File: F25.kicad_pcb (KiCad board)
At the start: 2 copper layers, 45 x 30 mm, 44 parts, among them J3 B2B-PH-K-S, J4 USB_C_Receptacle_USB2.0_16P, Q1 IRLML6244, SW1 RESET, SW2 BOOT, U1 MS5611-01BA, U2 MPU-6050, U4 ESP32-S3-WROOM-1-N8, U5 AP2112K-3.3

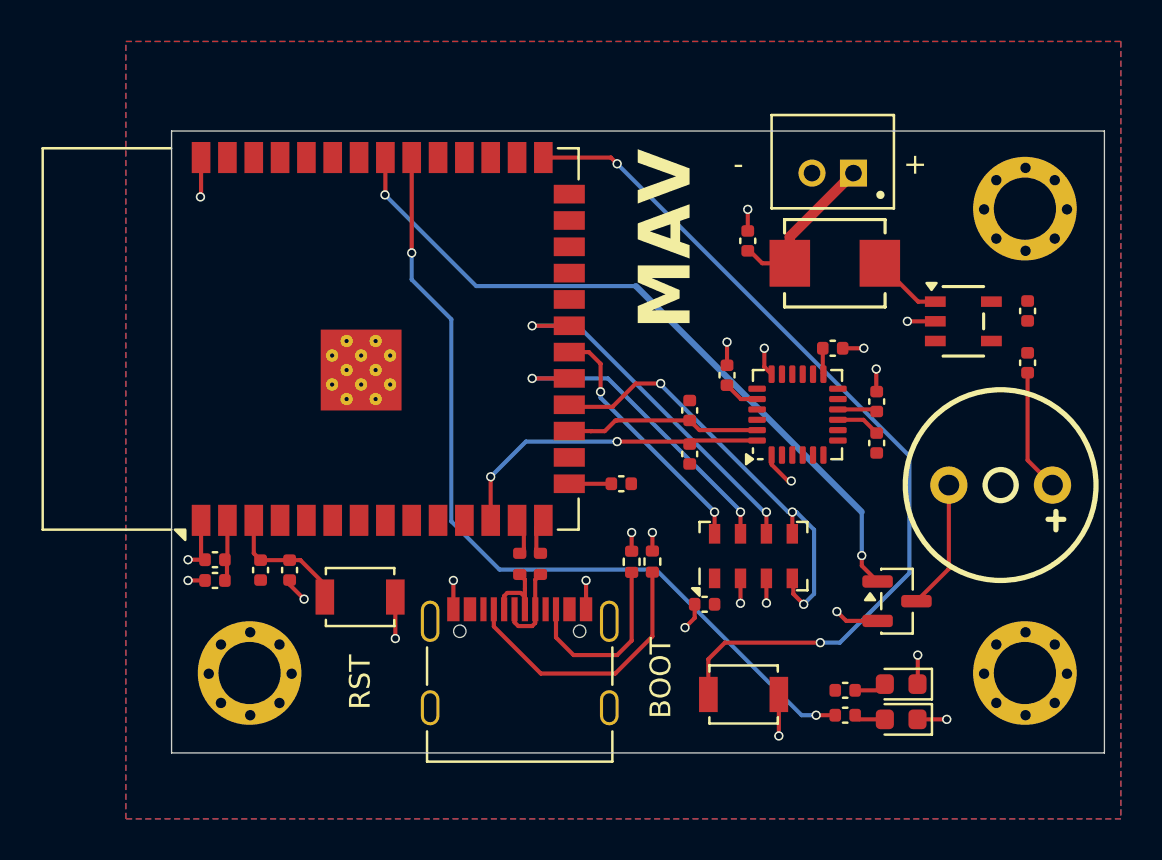
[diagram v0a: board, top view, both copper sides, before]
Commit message: Update LED Resistors
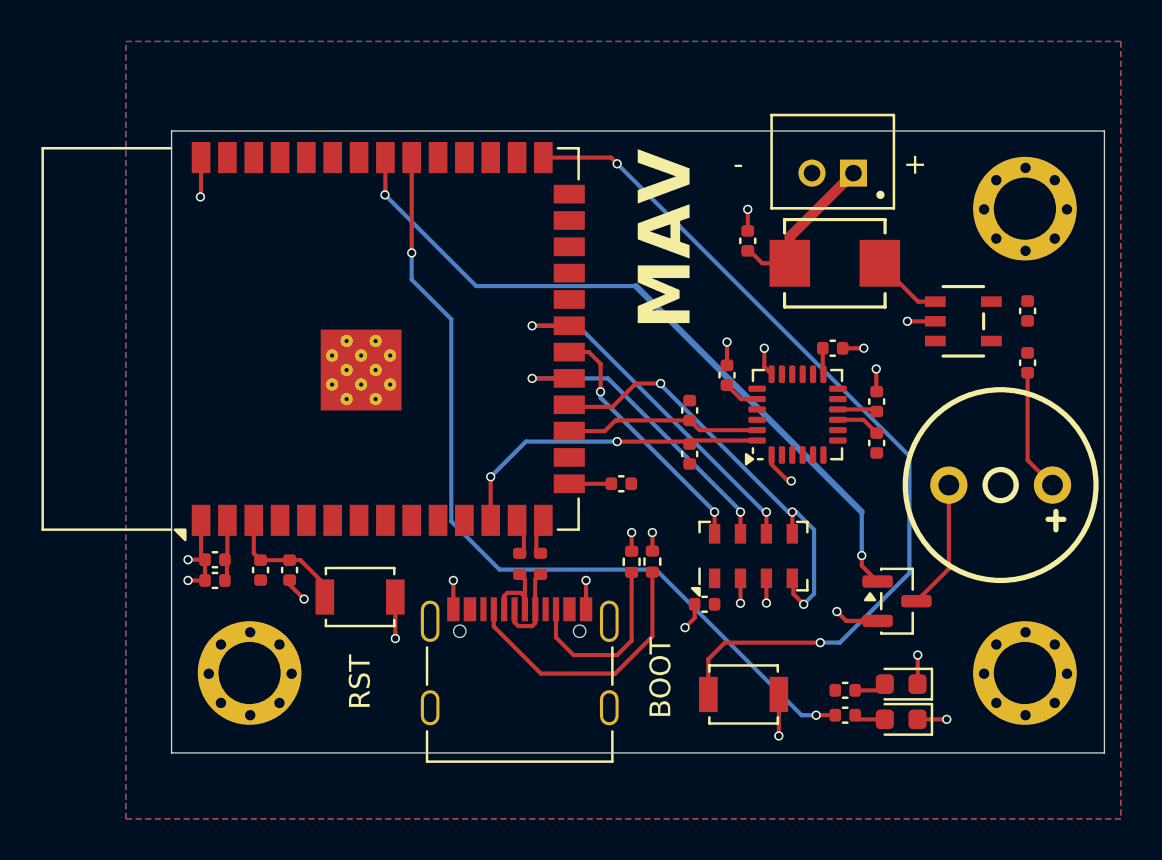
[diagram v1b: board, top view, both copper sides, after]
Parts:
- removed ?: , clipboard:8a0a766a-bff8-4b8c-9015-f6a2d7131c27
- R1: value 2k -> 270R
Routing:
- net BAT-: track 34.9 -> 35.9 mm

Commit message: LED Updates
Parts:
- R1: value 270R -> 120R
- R7: value 1.5k -> 820R
- moved G*** 0.44 mm to (154.6, 96.0)
- moved G*** 0.33 mm to (154.5, 93.0)
- moved G*** 0.32 mm to (153.0, 89.0)
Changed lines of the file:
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@@
 			)
 		)
-		(fp_text user "${REFERENCE}"
-			(at 0 -0.6 90)
-			(unlocked yes)
-			(layer "F.Fab")
-			(effects
-				(font
-					(size 1 1)
-					(thickness 0.15)
-				)
-			)
-		)
 		(pad "" smd rect
 			(at -2.9 1.06 90)
@@
 			)
 		)
-		(property "Value" "1.5k"
+		(property "Value" "820R"
 			(at 0 1.16 0)
 			(layer "F.Fab")
@@
 			)
 		)
-		(property "LCSC" "C25867"
+		(property "LCSC" "C25135"
 			(at 0 0 0)
 			(unlocked yes)
@@
 			)
 		)
-		(property "Value" "270R"
+		(property "Value" "120R"
 			(at 0 1.16 0)
 			(layer "F.Fab")
@@
 			)
 		)
-		(property "LCSC" "C25099"
+		(property "LCSC" "C25079"
 			(at 0 0 0)
 			(unlocked yes)
@@
 	(footprint "LOGO"
 		(layer "B.Cu")
-		(at 154.824101 93.082125)
+		(at 154.5 93)
 		(property "Reference" "G***"
 			(at 0 0 0)
@@
 	(footprint "LOGO"
 		(layer "B.Cu")
-		(at 155.024101 95.882125)
+		(at 154.6 96)
 		(property "Reference" "G***"
 			(at 0 0 0)
@@
 	(footprint "LOGO"
 		(layer "B.Cu")
-		(at 142.519024 94.578305)
+		(at 142.5 94.6)
 		(property "Reference" "G***"
 			(at 0 0 0)
@@
 	(footprint "LOGO"
 		(layer "B.Cu")
-		(at 153.1 89.3)
+		(at 153 89)
 		(property "Reference" "G***"
 			(at 0 0 0)

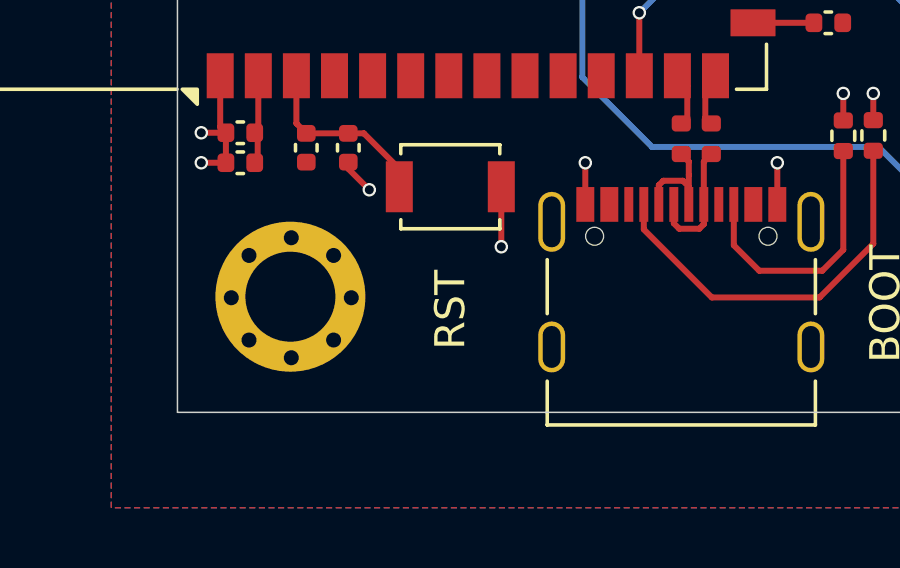
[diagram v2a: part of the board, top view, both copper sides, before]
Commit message: Fix LED Resistors and models
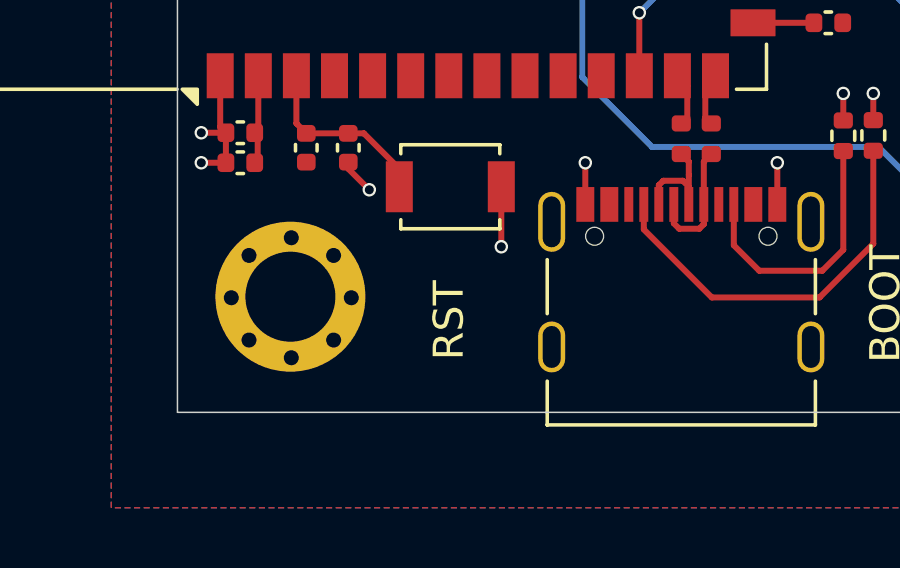
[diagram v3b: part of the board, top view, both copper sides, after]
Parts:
- R1: value 120R -> 1k
- R7: value 820R -> 2k
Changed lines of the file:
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@@
 			)
 		)
-		(property "Value" "820R"
+		(property "Value" "2k"
 			(at 0 1.16 0)
 			(layer "F.Fab")
@@
 			)
 		)
-		(property "LCSC" "C25135"
+		(property "LCSC" "C4109"
 			(at 0 0 0)
 			(unlocked yes)
@@
 			)
 		)
-		(property "Value" "120R"
+		(property "Value" "1k"
 			(at 0 1.16 0)
 			(layer "F.Fab")
@@
 			)
 		)
-		(property "LCSC" "C25079"
+		(property "LCSC" "C11702"
 			(at 0 0 0)
 			(unlocked yes)
@@
 	)
 	(gr_text "RST"
-		(at 144.8 111.9 90)
+		(at 144.75 112.25 90)
 		(layer "F.SilkS")
 		(effects
@@
 			(polygon
 				(pts
-					(xy 144.635228 112.589086) (xy 144.68255 112.594199) (xy 144.725302 112.604932) (xy 144.760647 112.622164)
-					(xy 144.790105 112.645517) (xy 144.809923 112.671196) (xy 144.826534 112.707204) (xy 144.855657 112.788799)
-					(xy 144.868249 112.724282) (xy 144.885428 112.677528) (xy 144.906032 112.644574) (xy 144.934599 112.620435)
-					(xy 144.976664 112.604443) (xy 145.037252 112.598351) (xy 145.218907 112.598351) (xy 145.218907 112.886801)
-					(xy 145.128232 112.886801) (xy 145.06239 112.89017) (xy 145.017712 112.898708) (xy 145.002204 112.907625)
-					(xy 144.989621 112.925875) (xy 144.980385 112.95785) (xy 144.976618 113.010022) (xy 144.976618 113.484586)
-					(xy 145.218907 113.484586) (xy 145.218907 113.768762) (xy 144.277107 113.768762) (xy 144.277107 113.011365)
-					(xy 144.507672 113.011365) (xy 144.507672 113.033775) (xy 144.507672 113.484586) (xy 144.746053 113.484586)
-					(xy 144.746053 113.054779) (xy 144.746053 113.018387) (xy 144.742317 112.953003) (xy 144.733566 112.916325)
-					(xy 144.722484 112.897976) (xy 144.704591 112.88645) (xy 144.671951 112.877764) (xy 144.617154 112.874162)
-					(xy 144.574457 112.876841) (xy 144.549255 112.88326) (xy 144.531007 112.896705) (xy 144.518785 112.921057)
-					(xy 144.509077 112.967951) (xy 144.507672 113.011365) (xy 144.277107 113.011365) (xy 144.277107 112.89938)
-					(xy 144.282223 112.81295) (xy 144.295958 112.7467) (xy 144.316423 112.696591) (xy 144.342564 112.659289)
-					(xy 144.377288 112.630379) (xy 144.424929 112.60791) (xy 144.48904 112.592823) (xy 144.574106 112.587177)
+					(xy 144.585228 112.939086) (xy 144.63255 112.944199) (xy 144.675302 112.954932) (xy 144.710647 112.972164)
+					(xy 144.740105 112.995517) (xy 144.759923 113.021196) (xy 144.776534 113.057204) (xy 144.805657 113.138799)
+					(xy 144.818249 113.074282) (xy 144.835428 113.027528) (xy 144.856032 112.994574) (xy 144.884599 112.970435)
+					(xy 144.926664 112.954443) (xy 144.987252 112.948351) (xy 145.168907 112.948351) (xy 145.168907 113.236801)
+					(xy 145.078232 113.236801) (xy 145.01239 113.24017) (xy 144.967712 113.248708) (xy 144.952204 113.257625)
+					(xy 144.939621 113.275875) (xy 144.930385 113.30785) (xy 144.926618 113.360022) (xy 144.926618 113.834586)
+					(xy 145.168907 113.834586) (xy 145.168907 114.118762) (xy 144.227107 114.118762) (xy 144.227107 113.361365)
+					(xy 144.457672 113.361365) (xy 144.457672 113.383775) (xy 144.457672 113.834586) (xy 144.696053 113.834586)
+					(xy 144.696053 113.404779) (xy 144.696053 113.368387) (xy 144.692317 113.303003) (xy 144.683566 113.266325)
+					(xy 144.672484 113.247976) (xy 144.654591 113.23645) (xy 144.621951 113.227764) (xy 144.567154 113.224162)
+					(xy 144.524457 113.226841) (xy 144.499255 113.23326) (xy 144.481007 113.246705) (xy 144.468785 113.271057)
+					(xy 144.459077 113.317951) (xy 144.457672 113.361365) (xy 144.227107 113.361365) (xy 144.227107 113.24938)
+					(xy 144.232223 113.16295) (xy 144.245958 113.0967) (xy 144.266423 113.046591) (xy 144.292564 113.009289)
+					(xy 144.327288 112.980379) (xy 144.374929 112.95791) (xy 144.43904 112.942823) (xy 144.524106 112.937177)
 				)
 			)
 			(polygon
 				(pts
-					(xy 144.933082 112.085319) (xy 144.968065 112.080377) (xy 144.99041 112.067434) (xy 145.003852 112.04685)
-					(xy 145.014154 112.004406) (xy 145.018262 111.93975) (xy 145.019605 111.805355) (xy 145.013927 111.614907)
-					(xy 145.010901 111.562109) (xy 145.003601 111.530346) (xy 144.994021 111.512752) (xy 144.969754 111.495408)
-					(xy 144.931495 111.488939) (xy 144.896748 111.495901) (xy 144.870434 111.516233) (xy 144.859182 111.536134)
-					(xy 144.850966 111.569056) (xy 144.847658 111.620524) (xy 144.847658 111.666747) (xy 144.83795 112.134289)
-					(xy 144.83296 112.200859) (xy 144.819474 112.251919) (xy 144.799018 112.290754) (xy 144.772065 112.319853)
-					(xy 144.73823 112.341674) (xy 144.69483 112.358515) (xy 144.639673 112.36963) (xy 144.570137 112.373708)
-					(xy 144.493601 112.369234) (xy 144.435168 112.357252) (xy 144.391168 112.339453) (xy 144.354399 112.311666)
-					(xy 144.325463 112.271212) (xy 144.304401 112.214828) (xy 144.287004 112.117455) (xy 144.277351 111.978218)
-					(xy 144.273199 111.781542) (xy 144.276008 111.582728) (xy 144.281312 111.469525) (xy 144.294876 111.390936)
-					(xy 144.311876 111.345248) (xy 144.334929 111.311755) (xy 144.363935 111.288049) (xy 144.413826 111.262508)
-					(xy 144.454672 111.249581) (xy 144.498929 111.243565) (xy 144.56629 111.241154) (xy 144.56629 111.519713)
-					(xy 144.534929 111.523377) (xy 144.512817 111.53316) (xy 144.497475 111.548412) (xy 144.483256 111.580794)
-					(xy 144.477814 111.62889) (xy 144.476409 111.766093) (xy 144.483248 111.983103) (xy 144.487436 112.024335)
-					(xy 144.499002 112.05662) (xy 144.511803 112.073289) (xy 144.528906 112.083192) (xy 144.551758 112.086723)
-					(xy 144.583244 112.082249) (xy 144.604406 112.070299) (xy 144.618131 112.051063) (xy 144.629455 112.011792)
-					(xy 144.633885 111.953733) (xy 144.633885 111.924301) (xy 144.636632 111.733914) (xy 144.638037 111.546336)
-					(xy 144.642542 111.452558) (xy 144.654633 111.380127) (xy 144.672528 111.325039) (xy 144.695006 111.283836)
-					(xy 144.726593 111.250997) (xy 144.772154 111.225608) (xy 144.835877 111.208449) (xy 144.923374 111.201953)
-					(xy 145.008351 111.207752) (xy 145.071604 111.223173) (xy 145.117945 111.246054) (xy 145.15113 111.27547)
-					(xy 145.175703 111.313128) (xy 145.195072 111.363801) (xy 145.208119 111.430871) (xy 145.212984 111.51837)
-					(xy 145.222815 111.882353) (xy 145.218663 112.07274) (xy 145.21486 112.15099) (xy 145.204596 112.212185)
-					(xy 145.189296 112.259419) (xy 145.169937 112.295367) (xy 145.142796 112.32404) (xy 145.10364 112.346162)
-					(xy 145.048883 112.361096) (xy 144.973688 112.366747) (xy 144.918 112.366747) (xy 144.918 112.086723)
+					(xy 144.883082 112.435319) (xy 144.918065 112.430377) (xy 144.94041 112.417434) (xy 144.953852 112.39685)
+					(xy 144.964154 112.354406) (xy 144.968262 112.28975) (xy 144.969605 112.155355) (xy 144.963927 111.964907)
+					(xy 144.960901 111.912109) (xy 144.953601 111.880346) (xy 144.944021 111.862752) (xy 144.919754 111.845408)
+					(xy 144.881495 111.838939) (xy 144.846748 111.845901) (xy 144.820434 111.866233) (xy 144.809182 111.886134)
+					(xy 144.800966 111.919056) (xy 144.797658 111.970524) (xy 144.797658 112.016747) (xy 144.78795 112.484289)
+					(xy 144.78296 112.550859) (xy 144.769474 112.601919) (xy 144.749018 112.640754) (xy 144.722065 112.669853)
+					(xy 144.68823 112.691674) (xy 144.64483 112.708515) (xy 144.589673 112.71963) (xy 144.520137 112.723708)
+					(xy 144.443601 112.719234) (xy 144.385168 112.707252) (xy 144.341168 112.689453) (xy 144.304399 112.661666)
+					(xy 144.275463 112.621212) (xy 144.254401 112.564828) (xy 144.237004 112.467455) (xy 144.227351 112.328218)
+					(xy 144.223199 112.131542) (xy 144.226008 111.932728) (xy 144.231312 111.819525) (xy 144.244876 111.740936)
+					(xy 144.261876 111.695248) (xy 144.284929 111.661755) (xy 144.313935 111.638049) (xy 144.363826 111.612508)
+					(xy 144.404672 111.599581) (xy 144.448929 111.593565) (xy 144.51629 111.591154) (xy 144.51629 111.869713)
+					(xy 144.484929 111.873377) (xy 144.462817 111.88316) (xy 144.447475 111.898412) (xy 144.433256 111.930794)
+					(xy 144.427814 111.97889) (xy 144.426409 112.116093) (xy 144.433248 112.333103) (xy 144.437436 112.374335)
+					(xy 144.449002 112.40662) (xy 144.461803 112.423289) (xy 144.478906 112.433192) (xy 144.501758 112.436723)
+					(xy 144.533244 112.432249) (xy 144.554406 112.420299) (xy 144.568131 112.401063) (xy 144.579455 112.361792)
+					(xy 144.583885 112.303733) (xy 144.583885 112.274301) (xy 144.586632 112.083914) (xy 144.588037 111.896336)
+					(xy 144.592542 111.802558) (xy 144.604633 111.730127) (xy 144.622528 111.675039) (xy 144.645006 111.633836)
+					(xy 144.676593 111.600997) (xy 144.722154 111.575608) (xy 144.785877 111.558449) (xy 144.873374 111.551953)
+					(xy 144.958351 111.557752) (xy 145.021604 111.573173) (xy 145.067945 111.596054) (xy 145.10113 111.62547)
+					(xy 145.125703 111.663128) (xy 145.145072 111.713801) (xy 145.158119 111.780871) (xy 145.162984 111.86837)
+					(xy 145.172815 112.232353) (xy 145.168663 112.42274) (xy 145.16486 112.50099) (xy 145.154596 112.562185)
+					(xy 145.139296 112.609419) (xy 145.119937 112.645367) (xy 145.092796 112.67404) (xy 145.05364 112.696162)
+					(xy 144.998883 112.711096) (xy 144.923688 112.716747) (xy 144.868 112.716747) (xy 144.868 112.436723)
 				)
 			)
 			(polygon
 				(pts
-					(xy 145.218907 110.646728) (xy 144.507672 110.646728) (xy 144.507672 111.063956) (xy 144.277107 111.063956)
-					(xy 144.277107 109.946728) (xy 144.507672 109.946728) (xy 144.507672 110.362552) (xy 145.218907 110.362552)
+					(xy 145.168907 110.996728) (xy 144.457672 110.996728) (xy 144.457672 111.413956) (xy 144.227107 111.413956)
+					(xy 144.227107 110.296728) (xy 144.457672 110.296728) (xy 144.457672 110.712552) (xy 145.168907 110.712552)
 				)
 			)

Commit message: Updates
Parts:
- removed G*** (x6): LOGO, LOGO
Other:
- board text removed: "Anthony D."
